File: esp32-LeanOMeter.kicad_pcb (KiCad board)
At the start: 2 copper layers, 92 x 68 mm, 4 parts, among them J1 Conn_01x06-SdCard, J2 Conn_02x15_Counter_Clockwise, J3 Conn_01x04-GpsModuleNeoM8N, J4 Conn_01x10-BNO085

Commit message: updated rx and tx values
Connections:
- J2 pad 21: unconnected-(J2-Pin_21-Pad21) -> Net-(J2-Pin_21)
- J2 pad 22: unconnected-(J2-Pin_22-Pad22) -> Net-(J2-Pin_22)
- J2 pad 27: Net-(J2-Pin_27) -> unconnected-(J2-Pin_27-Pad27)
- J2 pad 28: Net-(J2-Pin_28) -> unconnected-(J2-Pin_28-Pad28)
- J3 pad 2: Net-(J2-Pin_27) -> Net-(J2-Pin_22)
- J3 pad 3: Net-(J2-Pin_28) -> Net-(J2-Pin_21)
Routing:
- net Net-(J2-Pin_21): track 0.00 -> 69.9 mm, vias 0 -> 2
- net Net-(J2-Pin_22): track 0.00 -> 62.6 mm, vias 0 -> 2
- net Net-(J2-Pin_28): track 28.1 -> 0.00 mm
- net Net-(J2-Pin_27): track 28.0 -> 0.00 mm
- net Net-(J1-Pin_3): vias 2 -> 0
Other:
- outline, holes or cut-outs redrawn
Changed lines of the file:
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@@
 			(layers "*.Cu" "*.Mask")
 			(remove_unused_layers no)
-			(net "Net-(J2-Pin_27)")
+			(net "Net-(J2-Pin_22)")
 			(pinfunction "Pin_2_2")
 			(pintype "passive")
@@
 			(layers "*.Cu" "*.Mask")
 			(remove_unused_layers no)
-			(net "Net-(J2-Pin_28)")
+			(net "Net-(J2-Pin_21)")
 			(pinfunction "Pin_3_3")
 			(pintype "passive")
@@
 			)
 		)
+		(property "Sim.Library" "/home/miniflint/Téléchargements/doit-esp32-devkit-v1.lib"
+			(at 0 0 0)
+			(unlocked yes)
+			(layer "F.Fab")
+			(hide yes)
+			(effects
+				(font
+					(size 1 1)
+					(thickness 0.15)
+				)
+			)
+		)
 		(property ki_fp_filters "Connector*:*_2x??_*")
 		(sheetname "/")
@@
 			(keep_end_layers yes)
 			(zone_layer_connections)
-			(net "unconnected-(J2-Pin_21-Pad21)")
+			(net "Net-(J2-Pin_21)")
 			(pinfunction "Pin_21_21")
-			(pintype "passive+no_connect")
+			(pintype "passive")
 		)
 		(pad "22" thru_hole circle
@@
 			(keep_end_layers yes)
 			(zone_layer_connections)
-			(net "unconnected-(J2-Pin_22-Pad22)")
+			(net "Net-(J2-Pin_22)")
 			(pinfunction "Pin_22_22")
-			(pintype "passive+no_connect")
+			(pintype "passive")
 		)
 		(pad "23" thru_hole circle
@@
 			(keep_end_layers yes)
 			(zone_layer_connections)
-			(net "Net-(J2-Pin_27)")
+			(net "unconnected-(J2-Pin_27-Pad27)")
 			(pinfunction "Pin_27_27")
 			(pintype "passive")
@@
 			(keep_end_layers yes)
 			(zone_layer_connections)
-			(net "Net-(J2-Pin_28)")
+			(net "unconnected-(J2-Pin_28-Pad28)")
 			(pinfunction "Pin_28_28")
 			(pintype "passive")
@@
 		(layer "Edge.Cuts")
 	)
-	(gr_rect
-		(start 119.8 74.6)
-		(end 145.8 100.6)
-		(stroke
-			(width 0.2)
-			(type solid)
-		)
-		(fill no)
-		(layer "Edge.Cuts")
-	)
 	(gr_circle
 		(center 149.05 40)
@@
 	)
 	(segment
+		(start 94.22 63.22)
+		(end 107.86 76.86)
+		(width 0.2)
+		(layer "F.Cu")
+		(net "Net-(J1-Pin_3)")
+	)
+	(segment
 		(start 89.78 63.22)
 		(end 90 63)
@@
 	)
 	(segment
-		(start 99 68)
-		(end 107.86 76.86)
-		(width 0.2)
-		(layer "F.Cu")
-		(net "Net-(J1-Pin_3)")
-	)
-	(segment
 		(start 90 63)
 		(end 89 63)
@@
 	)
 	(segment
-		(start 94.22 63.22)
-		(end 95 64)
-		(width 0.2)
-		(layer "F.Cu")
-		(net "Net-(J1-Pin_3)")
-	)
-	(segment
 		(start 89.36 63.22)
 		(end 89.78 63.22)
@@
 		(net "Net-(J1-Pin_3)")
 	)
+	(segment
+		(start 104 87)
+		(end 105.32 85.68)
+		(width 0.2)
+		(layer "F.Cu")
+		(net "Net-(J1-Pin_4)")
+	)
+	(segment
+		(start 97.9 87)
+		(end 104 87)
+		(width 0.2)
+		(layer "F.Cu")
+		(net "Net-(J1-Pin_4)")
+	)
+	(segment
+		(start 89.36 78.46)
+		(end 97.9 87)
+		(width 0.2)
+		(layer "F.Cu")
+		(net "Net-(J1-Pin_4)")
+	)
+	(segment
+		(start 105.32 85.68)
+		(end 105.32 83.1225)
+		(width 0.2)
+		(layer "F.Cu")
+		(net "Net-(J1-Pin_4)")
+	)
+	(segment
+		(start 100.92 75.92)
+		(end 102.78 77.78)
+		(width 0.2)
+		(layer "F.Cu")
+		(net "Net-(J1-Pin_5)")
+	)
+	(segment
+		(start 102.78 77.78)
+		(end 102.78 83.1225)
+		(width 0.2)
+		(layer "F.Cu")
+		(net "Net-(J1-Pin_5)")
+	)
+	(segment
+		(start 89.36 75.92)
+		(end 100.92 75.92)
+		(width 0.2)
+		(layer "F.Cu")
+		(net "Net-(J1-Pin_5)")
+	)
+	(segment
+		(start 107.25 57)
+		(end 88 57)
+		(width 0.2)
+		(layer "F.Cu")
+		(net "Net-(J2-Pin_22)")
+	)
+	(segment
+		(start 80.25 76)
+		(end 80.25 57.5)
+		(width 0.2)
+		(layer "F.Cu")
+		(net "Net-(J2-Pin_22)")
+	)
+	(segment
+		(start 80.75 57)
+		(end 81.75 57)
+		(width 0.2)
+		(layer "F.Cu")
+		(net "Net-(J2-Pin_22)")
+	)
+	(segment
+		(start 89.5 83.5)
+		(end 87.75 83.5)
+		(width 0.2)
+		(layer "F.Cu")
+		(net "Net-(J2-Pin_22)")
+	)
+	(segment
+		(start 107.25 57)
+		(end 108.59 55.66)
+		(width 0.2)
+		(layer "F.Cu")
+		(net "Net-(J2-Pin_22)")
+	)
+	(segment
+		(start 89.36 83.54)
+		(end 89.46 83.54)
+		(width 0.2)
+		(layer "F.Cu")
+		(net "Net-(J2-Pin_22)")
+	)
+	(segment
+		(start 89.46 83.54)
+		(end 89.5 83.5)
+		(width 0.2)
+		(layer "F.Cu")
+		(net "Net-(J2-Pin_22)")
+	)
+	(segment
+		(start 80.25 57.5)
+		(end 80.75 57)
+		(width 0.2)
+		(layer "F.Cu")
+		(net "Net-(J2-Pin_22)")
+	)
+	(segment
+		(start 87.75 83.5)
+		(end 80.25 76)
+		(width 0.2)
+		(layer "F.Cu")
+		(net "Net-(J2-Pin_22)")
+	)
+	(segment
+		(start 108.59 55.66)
+		(end 111.1 55.66)
+		(width 0.2)
+		(layer "F.Cu")
+		(net "Net-(J2-Pin_22)")
+	)
 	(via
-		(at 99 68)
+		(at 81.75 57)
 		(size 0.6)
 		(drill 0.3)
 		(layers "F.Cu" "B.Cu")
-		(net "Net-(J1-Pin_3)")
+		(net "Net-(J2-Pin_22)")
 	)
 	(via
-		(at 95 64)
+		(at 88 57)
 		(size 0.6)
 		(drill 0.3)
 		(layers "F.Cu" "B.Cu")
-		(net "Net-(J1-Pin_3)")
-	)
-	(segment
-		(start 95 64)
-		(end 99 68)
+		(net "Net-(J2-Pin_22)")
+	)
+	(segment
+		(start 88 57)
+		(end 81.75 57)
 		(width 0.2)
 		(layer "B.Cu")
-		(net "Net-(J1-Pin_3)")
-	)
-	(segment
-		(start 104 87)
-		(end 105.32 85.68)
-		(width 0.2)
-		(layer "F.Cu")
-		(net "Net-(J1-Pin_4)")
-	)
-	(segment
-		(start 97.9 87)
-		(end 104 87)
-		(width 0.2)
-		(layer "F.Cu")
-		(net "Net-(J1-Pin_4)")
-	)
-	(segment
-		(start 89.36 78.46)
-		(end 97.9 87)
-		(width 0.2)
-		(layer "F.Cu")
-		(net "Net-(J1-Pin_4)")
-	)
-	(segment
-		(start 105.32 85.68)
-		(end 105.32 83.1225)
-		(width 0.2)
-		(layer "F.Cu")
-		(net "Net-(J1-Pin_4)")
-	)
-	(segment
-		(start 100.92 75.92)
-		(end 102.78 77.78)
-		(width 0.2)
-		(layer "F.Cu")
-		(net "Net-(J1-Pin_5)")
-	)
-	(segment
-		(start 102.78 77.78)
-		(end 102.78 83.1225)
-		(width 0.2)
-		(layer "F.Cu")
-		(net "Net-(J1-Pin_5)")
-	)
-	(segment
-		(start 89.36 75.92)
-		(end 100.92 75.92)
-		(width 0.2)
-		(layer "F.Cu")
-		(net "Net-(J1-Pin_5)")
-	)
-	(segment
-		(start 93.16 70.84)
-		(end 108.34 55.66)
-		(width 0.2)
-		(layer "F.Cu")
-		(net "Net-(J2-Pin_27)")
-	)
-	(segment
-		(start 89.36 70.84)
-		(end 93.16 70.84)
-		(width 0.2)
-		(layer "F.Cu")
-		(net "Net-(J2-Pin_27)")
-	)
-	(segment
-		(start 108.34 55.66)
-		(end 111.1 55.66)
-		(width 0.2)
-		(layer "F.Cu")
-		(net "Net-(J2-Pin_27)")
-	)
-	(segment
-		(start 89.36 68.3)
-		(end 92.7 68.3)
-		(width 0.2)
-		(layer "F.Cu")
-		(net "Net-(J2-Pin_28)")
-	)
-	(segment
-		(start 108 53)
-		(end 110.98 53)
-		(width 0.2)
-		(layer "F.Cu")
-		(net "Net-(J2-Pin_28)")
-	)
-	(segment
-		(start 92.7 68.3)
-		(end 108 53)
-		(width 0.2)
-		(layer "F.Cu")
-		(net "Net-(J2-Pin_28)")
+		(net "Net-(J2-Pin_22)")
+	)
+	(segment
+		(start 108.63 53.12)
+		(end 106.25 55.5)
+		(width 0.2)
+		(layer "F.Cu")
+		(net "Net-(J2-Pin_21)")
+	)
+	(segment
+		(start 78.25 56.5)
+		(end 79.25 55.5)
+		(width 0.2)
+		(layer "F.Cu")
+		(net "Net-(J2-Pin_21)")
+	)
+	(segment
+		(start 87.08 86.08)
+		(end 78.25 77.25)
+		(width 0.2)
+		(layer "F.Cu")
+		(net "Net-(J2-Pin_21)")
+	)
+	(segment
+		(start 111.1 53.12)
+		(end 108.63 53.12)
+		(width 0.2)
+		(layer "F.Cu")
+		(net "Net-(J2-Pin_21)")
+	)
+	(segment
+		(start 106.25 55.5)
+		(end 88 55.5)
+		(width 0.2)
+		(layer "F.Cu")
+		(net "Net-(J2-Pin_21)")
+	)
+	(segment
+		(start 79.25 55.5)
+		(end 81.75 55.5)
+		(width 0.2)
+		(layer "F.Cu")
+		(net "Net-(J2-Pin_21)")
 	)
 	(segment
@@
 		(width 0.2)
 		(layer "F.Cu")
-		(net "Net-(J2-Pin_28)")
+		(net "Net-(J2-Pin_21)")
+	)
+	(segment
+		(start 78.25 77.25)
+		(end 78.25 56.5)
+		(width 0.2)
+		(layer "F.Cu")
+		(net "Net-(J2-Pin_21)")
+	)
+	(segment
+		(start 89.36 86.08)
+		(end 87.08 86.08)
+		(width 0.2)
+		(layer "F.Cu")
+		(net "Net-(J2-Pin_21)")
+	)
+	(via
+		(at 88 55.5)
+		(size 0.6)
+		(drill 0.3)
+		(layers "F.Cu" "B.Cu")
+		(net "Net-(J2-Pin_21)")
+	)
+	(via
+		(at 81.75 55.5)
+		(size 0.6)
+		(drill 0.3)
+		(layers "F.Cu" "B.Cu")
+		(net "Net-(J2-Pin_21)")
+	)
+	(segment
+		(start 81.75 55.5)
+		(end 88 55.5)
+		(width 0.2)
+		(layer "B.Cu")
+		(net "Net-(J2-Pin_21)")
 	)
 	(zone

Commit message: track lengths fixed (for fun)
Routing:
- net Net-(J1-Pin_5): track 19.5 -> 30.0 mm
- net Net-(J2-Pin_29): track 24.2 -> 32.8 mm
- net Net-(J1-Pin_4): track 22.6 -> 29.5 mm
- net Net-(J2-Pin_22): track 62.6 -> 67.7 mm
- net Net-(J2-Pin_21): track 69.9 -> 67.9 mm

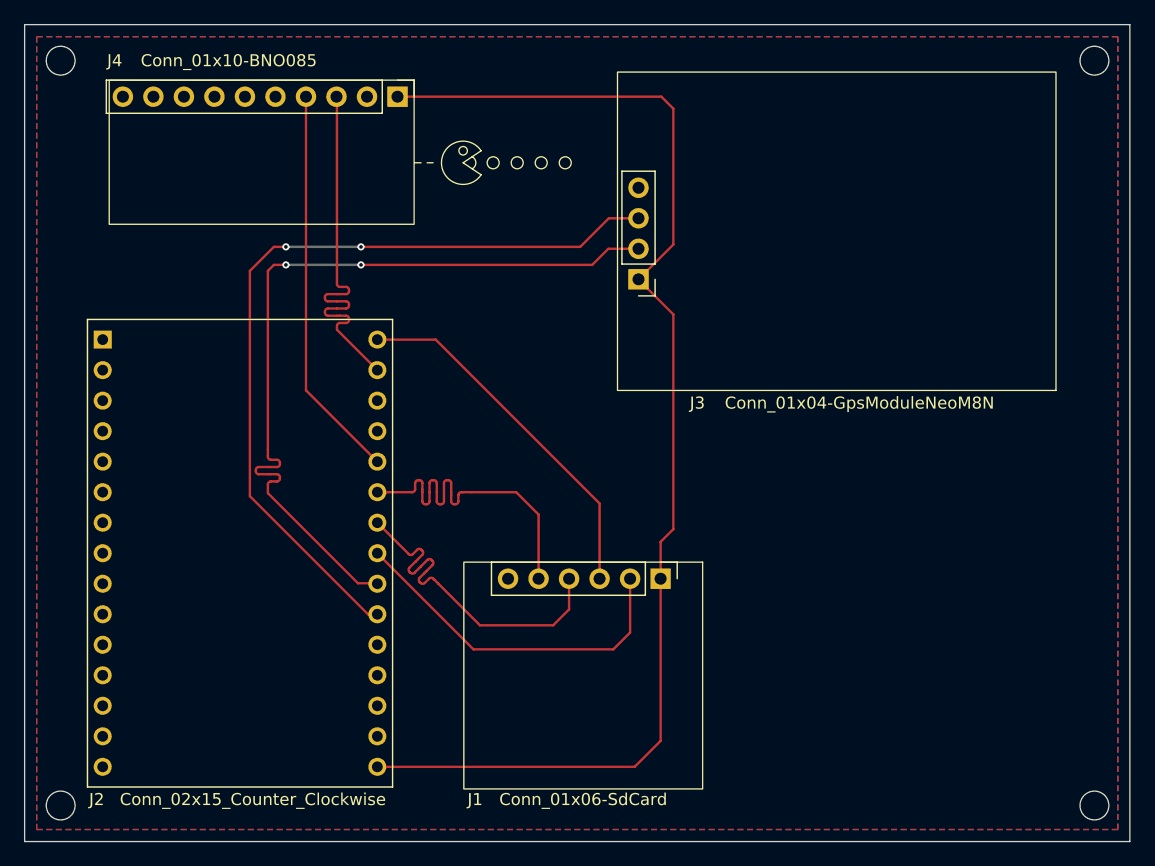
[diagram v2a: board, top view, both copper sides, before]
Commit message: fix: changed the gps module. added resistors, added capacitors
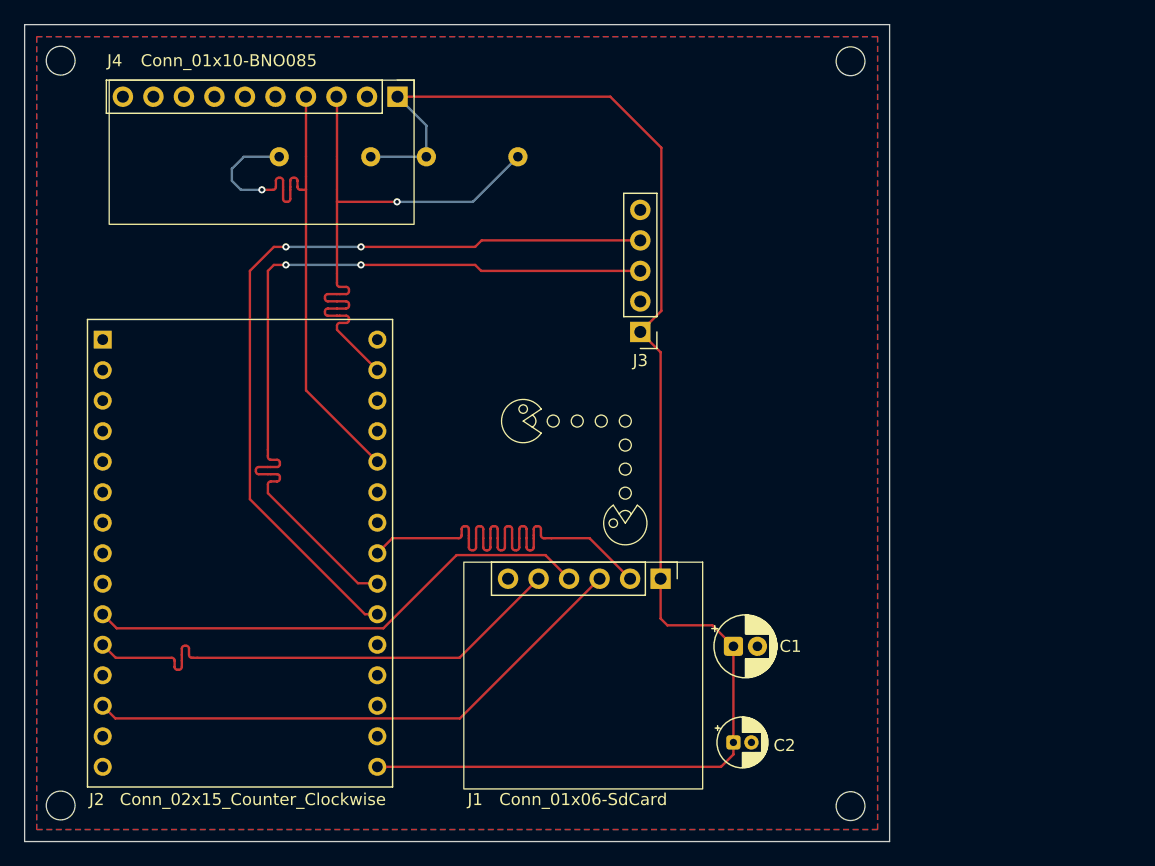
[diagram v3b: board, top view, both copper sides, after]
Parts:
- added C1: 10uF, Capacitor_THT:CP_Radial_D5.0mm_P2.00mm, F.Cu at (119.0, 88.8)
- added C2: 0.1uF, Capacitor_THT:CP_Radial_D4.0mm_P1.50mm, F.Cu at (119.0, 96.8)
- added R1: 4.7k, Resistor_THT:R_Axial_DIN0207_L6.3mm_D2.5mm_P7.62mm_Horizontal, B.Cu at (93.4, 48.0)
- added R2: 4.7k, Resistor_THT:R_Axial_DIN0207_L6.3mm_D2.5mm_P7.62mm_Horizontal, B.Cu at (88.8, 48.0)
- J3: value Conn_01x04-GpsModuleNeoM8N -> Conn_01x05_GpsModule; footprint Connector_PinHeader_2.54mm:PinHeader_1x04_P2.54mm_Vertical -> Connector_PinHeader_2.54mm:PinHeader_1x05_P2.54mm_Vertical
- moved J3 4.38 mm to (111.2, 62.6)
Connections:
- net Net-(J1-Pin_1) renamed +3.3V
- net Net-(J1-Pin_2) renamed CS/SS
- net Net-(J2-Pin_26) renamed SDA
- net Net-(J2-Pin_29) renamed SCL
- J1 pad 3: Net-(J1-Pin_3) -> MOSI
- J1 pad 4: Net-(J1-Pin_4) -> CLK
- J1 pad 5: Net-(J1-Pin_5) -> MISO
- J1 pad 6: Net-(J1-Pin_6) -> GND
- J2 pad 10: unconnected-(J2-Pin_10-Pad10) -> CLK
- J2 pad 11: unconnected-(J2-Pin_11-Pad11) -> MISO
- J2 pad 13: unconnected-(J2-Pin_13-Pad13) -> MOSI
- J2 pad 17: Net-(J1-Pin_6) -> GND
- J2 pad 21: Net-(J2-Pin_21) -> RX
- J2 pad 22: Net-(J2-Pin_22) -> TX
- J2 pad 24: Net-(J1-Pin_4) -> unconnected-(J2-Pin_24-Pad24)
- J2 pad 25: Net-(J1-Pin_5) -> unconnected-(J2-Pin_25-Pad25)
- J2 pad 30: Net-(J1-Pin_3) -> unconnected-(J2-Pin_30-Pad30)
- J3 pad 2: Net-(J2-Pin_22) -> GND
- J3 pad 3: Net-(J2-Pin_21) -> TX
- J3 pad 4: Net-(J1-Pin_6) -> RX
- J4 pad 2: Net-(J1-Pin_6) -> GND
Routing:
- net Net-(J2-Pin_21): track 67.9 -> 0.00 mm, vias 2 -> 0
- net Net-(J2-Pin_22): track 67.7 -> 0.00 mm, vias 2 -> 0
- net TX: track 0.00 -> 67.6 mm, vias 0 -> 2
- net RX: track 0.00 -> 67.2 mm, vias 0 -> 2
- net MOSI: track 0.00 -> 46.6 mm
- net MISO: track 0.00 -> 42.8 mm
- net CLK: track 0.00 -> 42.6 mm
- net Net-(J1-Pin_3): track 32.3 -> 0.00 mm
- net Net-(J1-Pin_5): track 30.0 -> 0.00 mm
- net Net-(J1-Pin_4): track 29.5 -> 0.00 mm
- net +3.3V: track 103.3 -> 121.1 mm
- net SDA: track 32.8 -> 49.8 mm, vias 0 -> 1
- net SCL: track 32.8 -> 49.4 mm, vias 0 -> 1
- net CS/SS: track 29.4 -> 42.3 mm
- net unconnected-(J2-Pin_30-Pad30): track 0.00 -> 1.87 mm
- added copper zone on B.Cu, net GND
- added copper zone on F.Cu, net GND
- removed copper zone on B.Cu, net Net-(J1-Pin_6)
- removed copper zone on F.Cu, net Net-(J1-Pin_6)
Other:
- board size 92 x 68 mm -> 72 x 68 mm
